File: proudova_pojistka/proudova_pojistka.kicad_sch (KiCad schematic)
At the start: 0 parts

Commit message: Schéma + Footprinty
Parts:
- added C11, C12, C15, C16, C18, C19, C20, C21, C6: 100n, Capacitor_THT:C_Disc_D5.0mm_W2.5mm_P5.00mm, symbol Device:C_Small
- added C13, C14: 1u, Capacitor_THT:C_Disc_D5.0mm_W2.5mm_P5.00mm, symbol Device:C_Small
- added C17, C22, C23: 220u/25, Capacitor_THT:CP_Radial_D8.0mm_P3.50mm, symbol Device:C_Polarized_Small
- added D3: ZD15V/0,5 W, Diode_THT:D_DO-41_SOD81_P7.62mm_Horizontal, symbol Device:D_Zener_Small
- added D4: LEDR, LED_THT:LED_D5.0mm, symbol Device:LED_Small
- added D5: LEDG, LED_THT:LED_D5.0mm, symbol Device:LED_Small
- added D6, D7: 1N4148, Diode_THT:D_DO-35_SOD27_P7.62mm_Horizontal, symbol Diode:1N4148
- added J2: Pojistka, TerminalBlock_Phoenix:TerminalBlock_Phoenix_MKDS-1,5-2-5.08_1x02_P5.08mm_Horizontal, symbol Connector:Screw_Terminal_01x02
- added J3: Napájení +12V, TerminalBlock_Phoenix:TerminalBlock_Phoenix_MKDS-1,5-2-5.08_1x02_P5.08mm_Horizontal, symbol Connector:Screw_Terminal_01x02
- added Q1: Q_NMOS_GDS, Package_TO_SOT_THT:TO-220-3_Vertical, symbol Device:Q_NMOS_GDS
- added Q2, Q5, Q6, Q7: BS170, Package_TO_SOT_THT:TO-92_Inline, symbol Transistor_FET:BS170
- added R10, R16: 100, Resistor_THT:R_Axial_DIN0207_L6.3mm_D2.5mm_P7.62mm_Horizontal, symbol Device:R_Small
- added R11: 270k, Resistor_THT:R_Axial_DIN0207_L6.3mm_D2.5mm_P7.62mm_Horizontal, symbol Device:R_Small
- added R12: 15k, Resistor_THT:R_Axial_DIN0207_L6.3mm_D2.5mm_P7.62mm_Horizontal, symbol Device:R_Small
- added R13, R14, R15, R22, R23, R24, R4, R8, R9: 1k, Resistor_THT:R_Axial_DIN0207_L6.3mm_D2.5mm_P7.62mm_Horizontal, symbol Device:R_Small
- added R17, R19, R20: 10k, Resistor_THT:R_Axial_DIN0207_L6.3mm_D2.5mm_P7.62mm_Horizontal, symbol Device:R_Small
- added R18: 0,1/3 W, Resistor_THT:R_Axial_DIN0918_L18.0mm_D9.0mm_P22.86mm_Horizontal, symbol Device:R_Small
- added R2: 5k1, Resistor_THT:R_Axial_DIN0207_L6.3mm_D2.5mm_P7.62mm_Horizontal, symbol Device:R_Small
- added R21, R7: 200, Resistor_THT:R_Axial_DIN0207_L6.3mm_D2.5mm_P7.62mm_Horizontal, symbol Device:R_Small
- added R3: 2k, Resistor_THT:R_Axial_DIN0207_L6.3mm_D2.5mm_P7.62mm_Horizontal, symbol Device:R_Small
- added R5: 510, Resistor_THT:R_Axial_DIN0207_L6.3mm_D2.5mm_P7.62mm_Horizontal, symbol Device:R_Small
- added R6: 330, Resistor_THT:R_Axial_DIN0207_L6.3mm_D2.5mm_P7.62mm_Horizontal, symbol Device:R_Small
- added SW1: ROZSAH, Button_Switch_THT:SW_DIP_SPSTx08_Slide_9.78x22.5mm_W7.62mm_P2.54mm, symbol Switch:SW_DIP_x08
- added SW2: SW_Push, Button_Switch_THT:SW_PUSH_6mm, symbol Switch:SW_Push
- added U3: LM311, Package_DIP:DIP-8_W7.62mm, symbol Comparator:LM311
- added U4: OP07, Package_DIP:DIP-8_W7.62mm, symbol Amplifier_Operational:OP07
- added U5: L78L05_SOT89, Package_TO_SOT_SMD:SOT-89-3, symbol Regulator_Linear:L78L05_SOT89
- added U6: NE555P, Package_DIP:DIP-8_W7.62mm, symbol Timer:NE555P
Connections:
- new net: R11.2, R9.1, U3.2 (+)
- new net: R14.2, U3.3 (-)
- new net: Q2.2 (G), Q5.1 (D), Q6.2 (G), R11.1, R20.1, U3.7
- new net: C13.1, R12.1, R13.2, U4.2 (-)
- new net: C13.2, R12.2, R14.1, U4.6
- new net: J2.2 (Pin_2), Q1.2 (D)
- new net: C22.2, D6.2 (A), D7.1 (K)
- new net: R10.1, R2.1, R3.1, R4.1, R5.1, R6.1, R7.1, R8.2, R9.2
- new net: R2.2, SW1.2
- new net: Q2.1 (D), Q5.2 (G), Q7.2 (G), R19.1, R21.2, SW2.2
- new net: Q6.3 (S), R16.1, R22.2
- new net: D3.1 (K), Q1.1 (G), R16.2, R17.2
- new net: C21.1, R24.2, U6.2 (TR), U6.6 (THR)
- new net: C22.1, R24.1, U6.3 (Q)
- new net: C20.1, U6.5 (CV)
- new net: C14.1, R21.1
- new net: R5.2, SW1.5
- new net: R7.2, SW1.7
- new net: Q1.3 (S), R15.1, R18.2
- new net: R15.2, U4.3 (+)
- new net: D5.2 (A), R22.1
- new net: R10.2, SW1.8
- new net: R4.2, SW1.4
- new net: Q7.1 (D), R23.1
- new net: D4.1 (K), R23.2
- new net: R3.2, SW1.3
- new net: R6.2, SW1.6
- new net +12V: C11.1, C15.1, C16.1, C17.1, C19.1, C6.1, D4.2 (A), J3.2 (Pin_2), Q6.1 (D), R19.2, R20.2, U3.8 (V+), U4.7 (V+), U5.3 (IN), U6.4 (R), U6.8 (VCC)
- new net +5V: C18.1, R8.1, U5.1 (OUT)
- new net -10V: C12.1, C23.2, D7.2 (A), U4.4 (V-)
- new net GND: C11.2, C12.2, C14.2, C15.2, C16.2, C17.2, C18.2, C19.2, C20.2, C21.2, C23.1, C6.2, D3.2 (A), D5.1 (K), D6.1 (K), J2.1 (Pin_1), J3.1 (Pin_1), Q2.3 (S), Q5.3 (S), Q7.3 (S), R13.1, R17.1, R18.1, SW1.10, SW1.11, SW1.12, SW1.13, SW1.14, SW1.15, SW1.16, SW1.9, SW2.1, U3.1 (GND), U3.4 (V-), U5.2 (GND), U6.1 (GND)
- no-connect marks 0 -> 6
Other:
- removed sheet Napajeni
- removed sheet Napajeni2
- note added: "0,25 A"
- note added: "0,5 A"
- note added: "0,75 A"
- note added: "1,5 A"
- note added: "2 A"
- note added: "2,5 A"
- note added: "3 A"
- note added: "START"

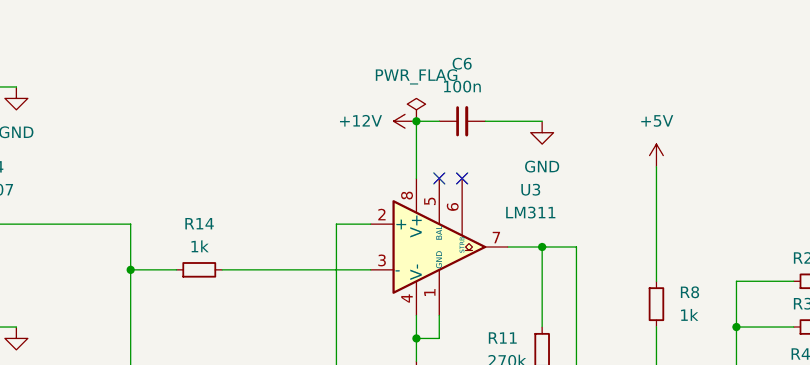
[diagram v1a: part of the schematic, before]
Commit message: Odevzdaná verze - Přidaný ground plane
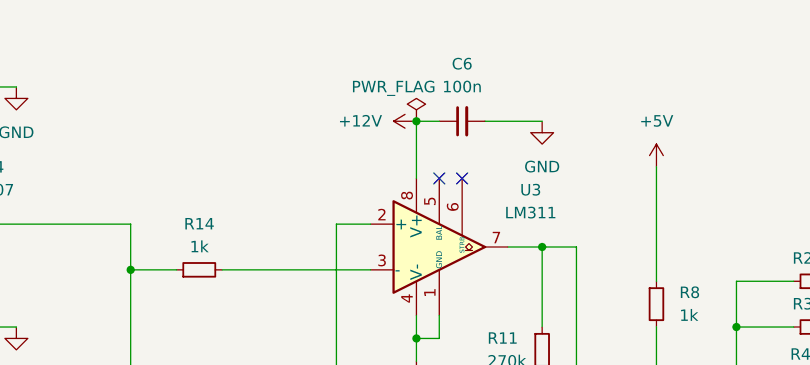
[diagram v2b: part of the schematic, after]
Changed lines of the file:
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@@
 		(on_board yes)
 		(dnp no)
-		(fields_autoplaced yes)
 		(property "Reference" "#FLG03"
 			(at 186.69 27.305 0)
@@
 		)
 		(property "Value" "PWR_FLAG"
-			(at 186.69 24.13 0)
+			(at 184.15 25.4 0)
 			(effects
 				(font
